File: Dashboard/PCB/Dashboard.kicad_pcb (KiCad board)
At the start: 4 copper layers, 96 parts, among them J1 Display, J2 Conn_01x26_Female, J3 LED, J7 PROGRAMMER, SW1 SW_SPST, U1 STM32F767ZIT6, U10 24LC01, U2 MP2359DJ-LF-Z, U3 MP2359DJ-LF-Z, U4 AS4C1M16S-6TCN, U5 AT25SF128A-SHB-T, U6 MP2332H, U7 MCP2561-E-SN, U8 MCP2561-E-SN, U9 ESP-12S, Y1 Crystal_GND24

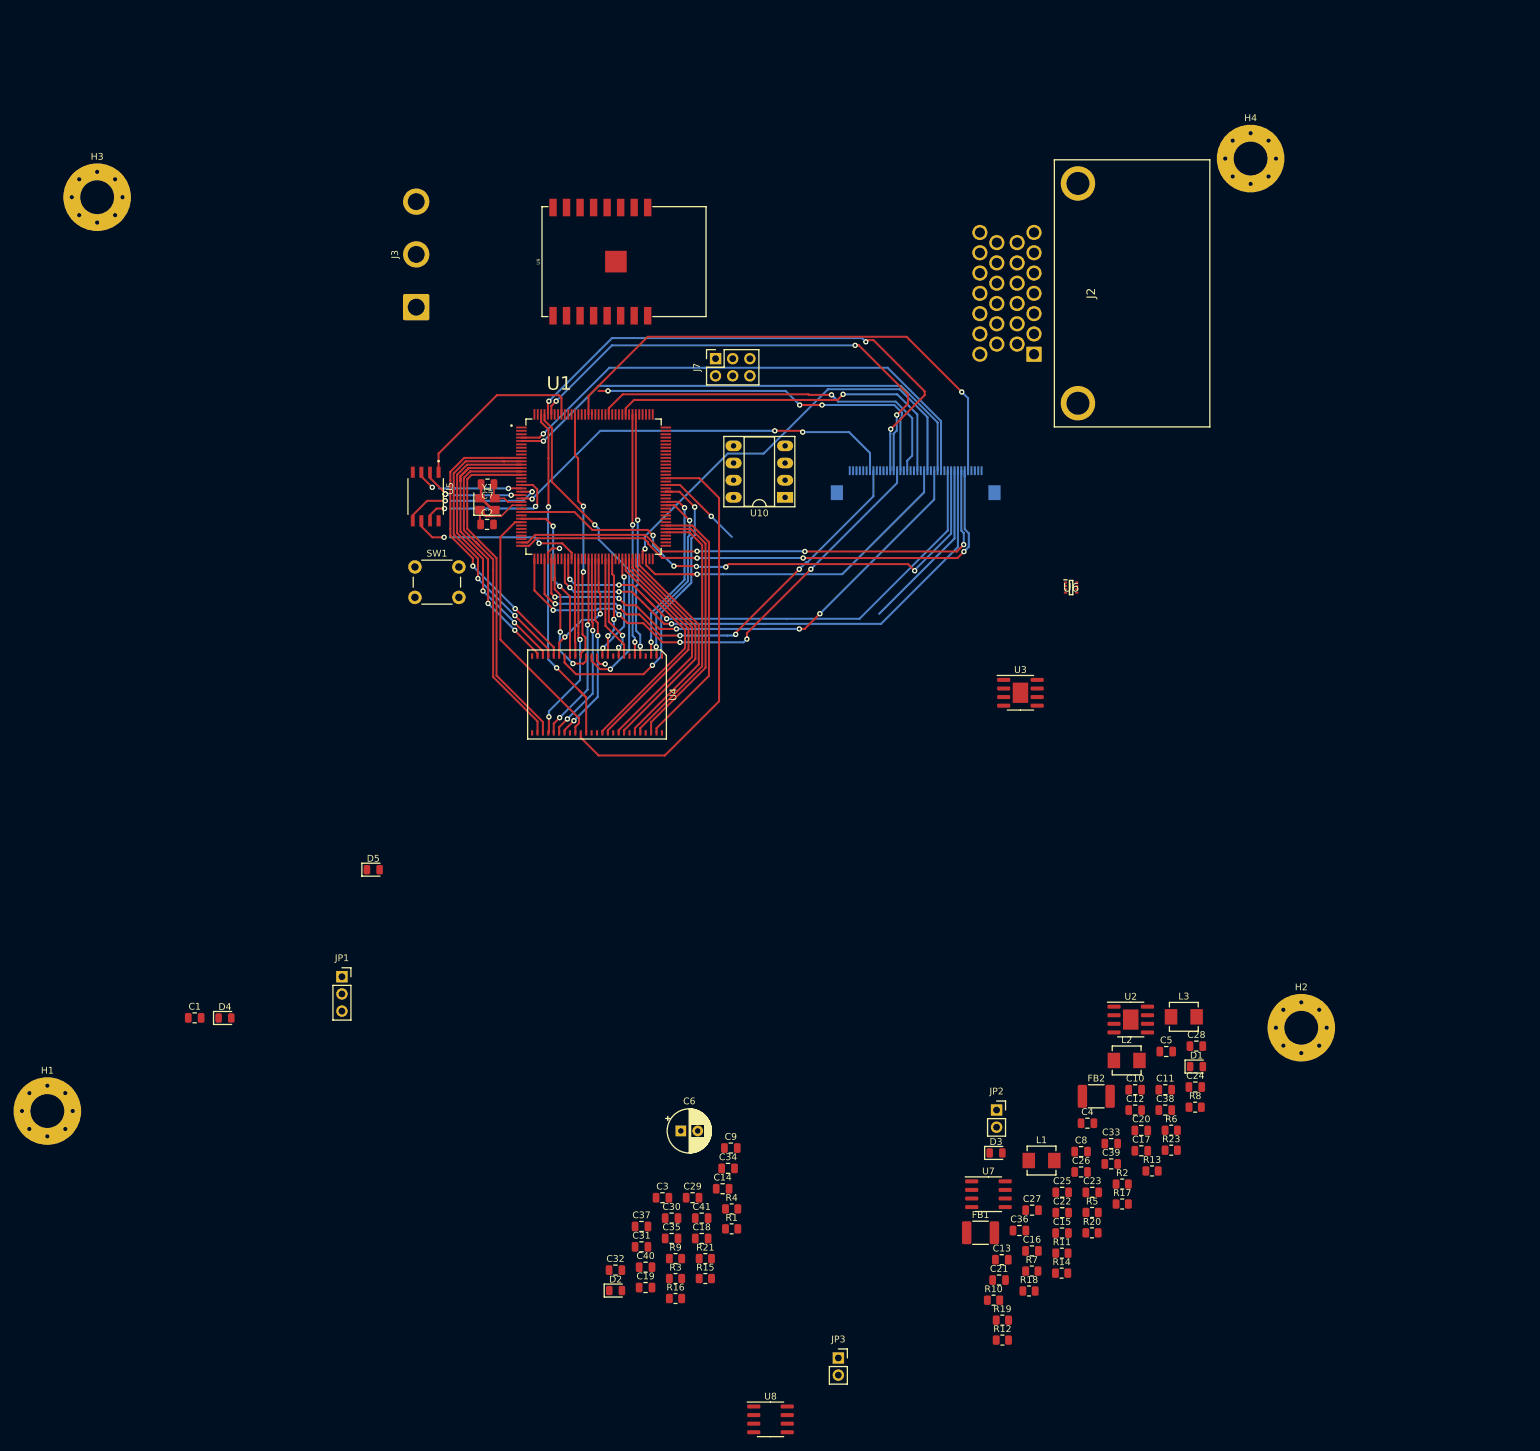
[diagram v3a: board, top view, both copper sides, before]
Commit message: New pcb board
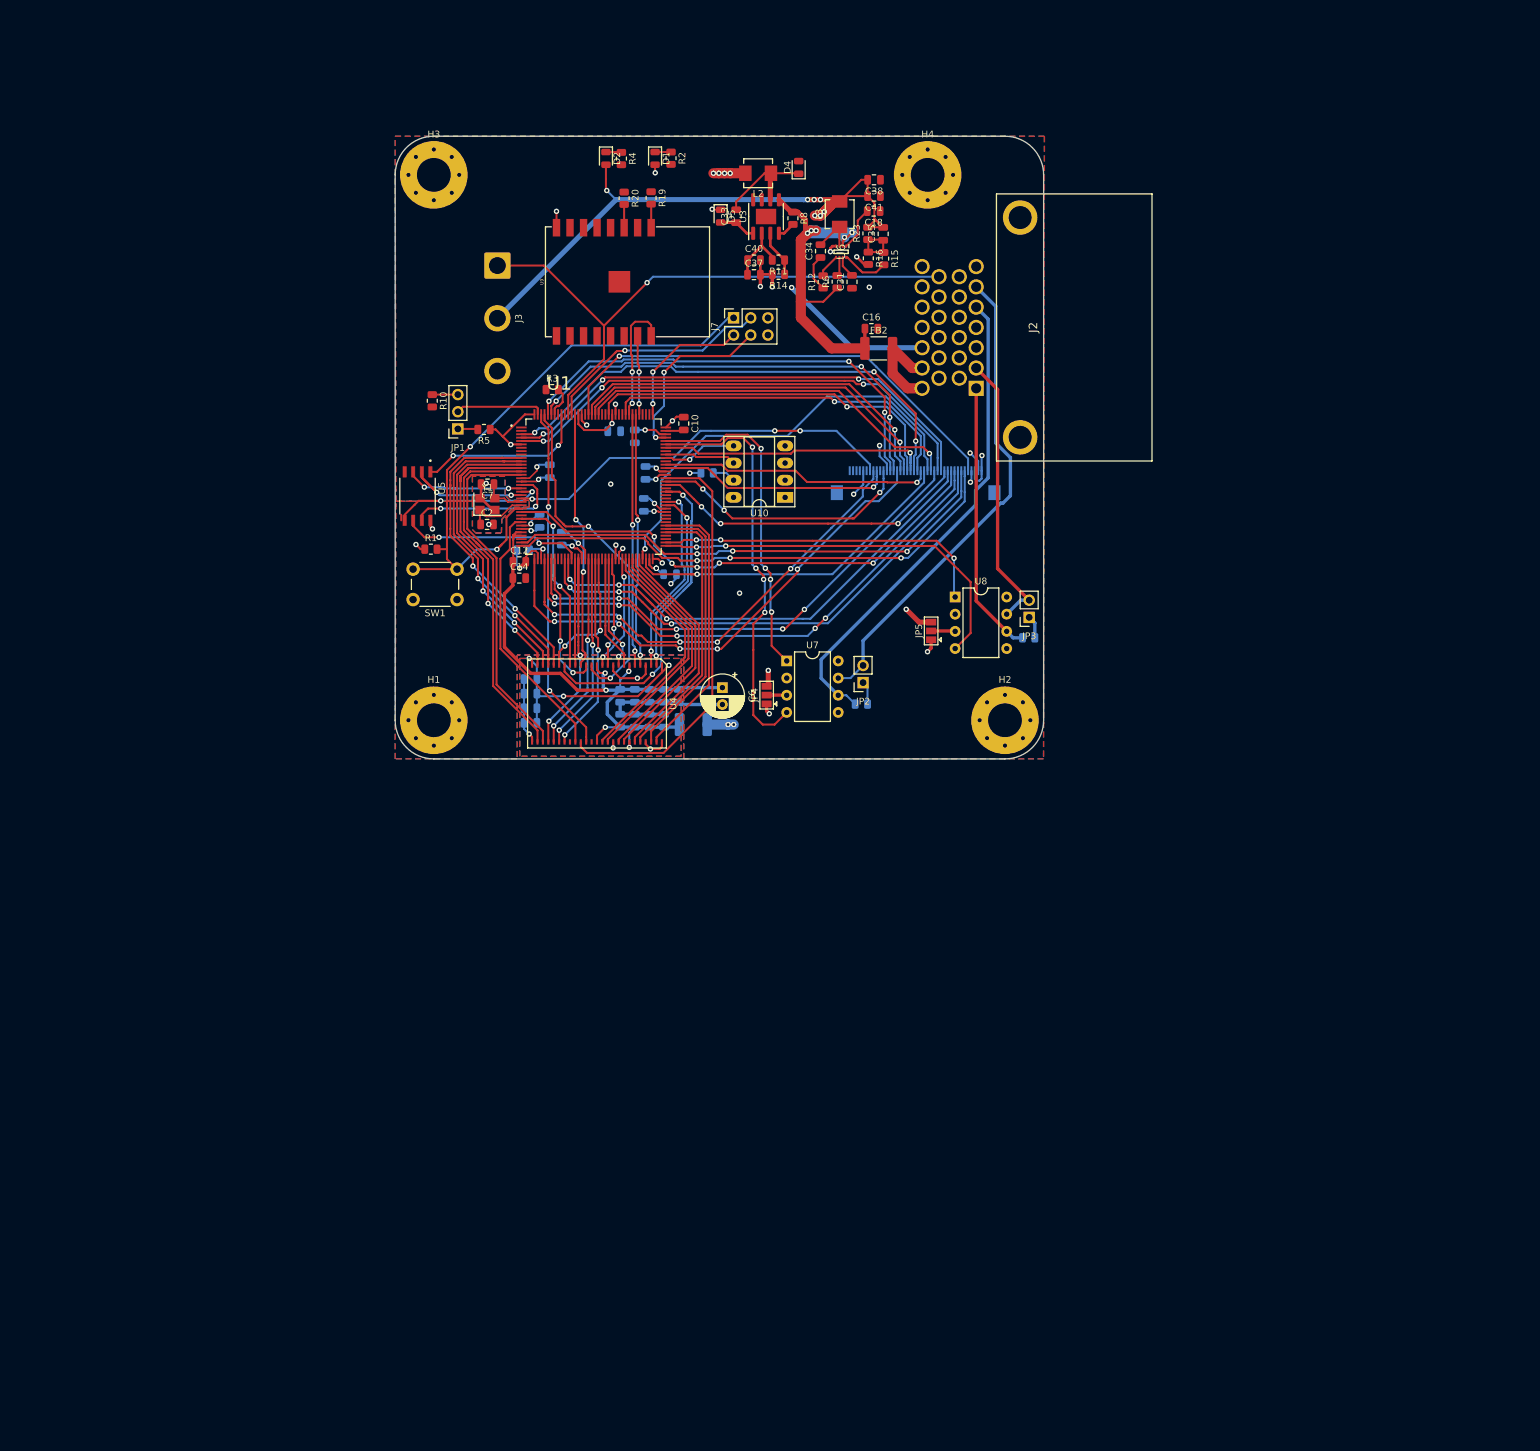
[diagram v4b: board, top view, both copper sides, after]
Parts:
- removed C32: 10nF, Capacitor_SMD:C_0805_2012Metric
- removed C36, C39: 10uF, Capacitor_SMD:C_0805_2012Metric
- removed D3: D_Schottky, Diode_SMD:D_0805_2012Metric
- removed L1: 10uH, Inductor_SMD:L_Vishay_IHLP-1616
- removed R13, R9: R, Resistor_SMD:R_0805_2012Metric
- removed R7: 100k, Resistor_SMD:R_0805_2012Metric
- removed U2: MP2359DJ-LF-Z, Package_SO:SOIC-8-1EP_3.9x4.9mm_P1.27mm_EP2.29x3mm
- added G***: LOGO, PGR_logo:logo_big, B.Cu at (133.1, 71.1)
- added JP4: Jumper_3_Bridged12, Jumper:SolderJumper-3_P1.3mm_Open_Pad1.0x1.5mm, F.Cu at (152.1, 111.9)
- added JP5: Jumper_3_Bridged12, Jumper:SolderJumper-3_P1.3mm_Open_Pad1.0x1.5mm, F.Cu at (176.4, 102.4)
- C1, C11, C13, C15, C17, C19, C20, C21, C22, C23, C24, C25, C26, C27, C28, C29, C3, C30, C4, C5, C8, C9, FB1, R17, R18, R21: moved to B.Cu
- U7, U8: footprint Package_SO:SOIC-8_3.9x4.9mm_P1.27mm -> Package_DIP:DIP-8_W7.62mm
- moved R19 173.9 mm to (135.0, 38.3), turned to 270 degrees
- moved R20 167.9 mm to (131.0, 38.4), turned to 270 degrees
- moved D2 167.4 mm to (128.3, 32.5), turned to 270 degrees
- moved R2 165.7 mm to (137.9, 32.5), turned to 270 degrees
- moved R12 158.7 mm to (160.4, 50.7), turned to 90 degrees
- moved R10 156.8 mm to (102.6, 68.3), turned to 270 degrees
- moved R16 156.4 mm to (167.1, 47.3), turned to 270 degrees
- moved D1 156.3 mm to (135.6, 32.5), turned to 270 degrees
- moved R4 156.2 mm to (130.6, 32.5), turned to 270 degrees
- moved C18 154.0 mm to (167.9, 40.3), turned to 180 degrees
- moved R14 153.5 mm to (153.8, 49.6), turned to 180 degrees
- moved C41 153.3 mm to (168.0, 38.1), turned to 180 degrees
- moved R15 153.1 mm to (169.4, 47.3), turned to 270 degrees
- moved R11 152.7 mm to (153.8, 47.5), turned to 180 degrees
- moved C35 151.8 mm to (169.3, 43.6), turned to 90 degrees
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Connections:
- J2 pad 1: Net-(J2-Pad1) -> CAN_L2
- J2 pad 12: GND -> Net-(J2-Pad12)
- J2 pad 13: GND -> Net-(J2-Pad13)
- J2 pad 15: +3V3 -> Net-(J2-Pad15)
- J2 pad 16: +5V -> Net-(J2-Pad16)
- J2 pad 17: +12V -> Net-(J2-Pad17)
- J2 pad 18: +12V -> Net-(J2-Pad18)
- J2 pad 19: Net-(J2-Pad19) -> LED_DATA
- J2 pad 2: Net-(J2-Pad2) -> CAN_H2
- J2 pad 22: Net-(J2-Pad22) -> GND
- J2 pad 23: CAN_L2 -> +3V3
- J2 pad 24: CAN_H2 -> +5V
- J2 pad 25: CAN_L1 -> +12V
- J2 pad 26: CAN_H1 -> +12V
- J2 pad 5: Net-(J2-Pad5) -> CAN_L1
- J2 pad 6: Net-(J2-Pad6) -> CAN_H1
- U7 pad 3: +5V -> Net-(JP4-Pad2)
- U8 pad 3: +5V -> Net-(JP5-Pad2)
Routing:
- net +5V: track 0.00 -> 255.2 mm, vias 0 -> 11
- net +3V3: track 0.00 -> 119.0 mm, vias 0 -> 30
- net GND: track 5.40 -> 122.4 mm, vias 0 -> 25
- net RST: track 0.00 -> 91.1 mm, vias 0 -> 2
- net +3.3VA: track 2.10 -> 91.8 mm, vias 1 -> 5
- net LED_DATA: track 0.00 -> 87.3 mm, vias 0 -> 1
- net /LTDC_B0: track 0.00 -> 73.9 mm, vias 0 -> 3
- net CAN_L1: track 0.00 -> 72.4 mm
- net CAN_H1: track 0.00 -> 71.8 mm
- net CAN_1_2: track 0.00 -> 61.1 mm, vias 0 -> 4
- net +12L: track 0.00 -> 59.8 mm, vias 0 -> 5
- net CAN_2_2: track 0.00 -> 58.2 mm, vias 0 -> 2
- net /LTDC_G3: track 0.00 -> 58.0 mm, vias 0 -> 1
- net /LTDC_B3: track 0.00 -> 55.2 mm, vias 0 -> 1
- net /LTDC_R4: track 28.7 -> 79.9 mm, vias 1 -> 5
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- added copper zone on In2.Cu, net +3V3
- added copper zone on B.Cu, net GND
- added copper zone on F.Cu, net GND
- added copper zone on In1.Cu, net GND
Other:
- board outline added: 95.9 x 92.1 mm
- board text added: "M. NADARZYNSKI"

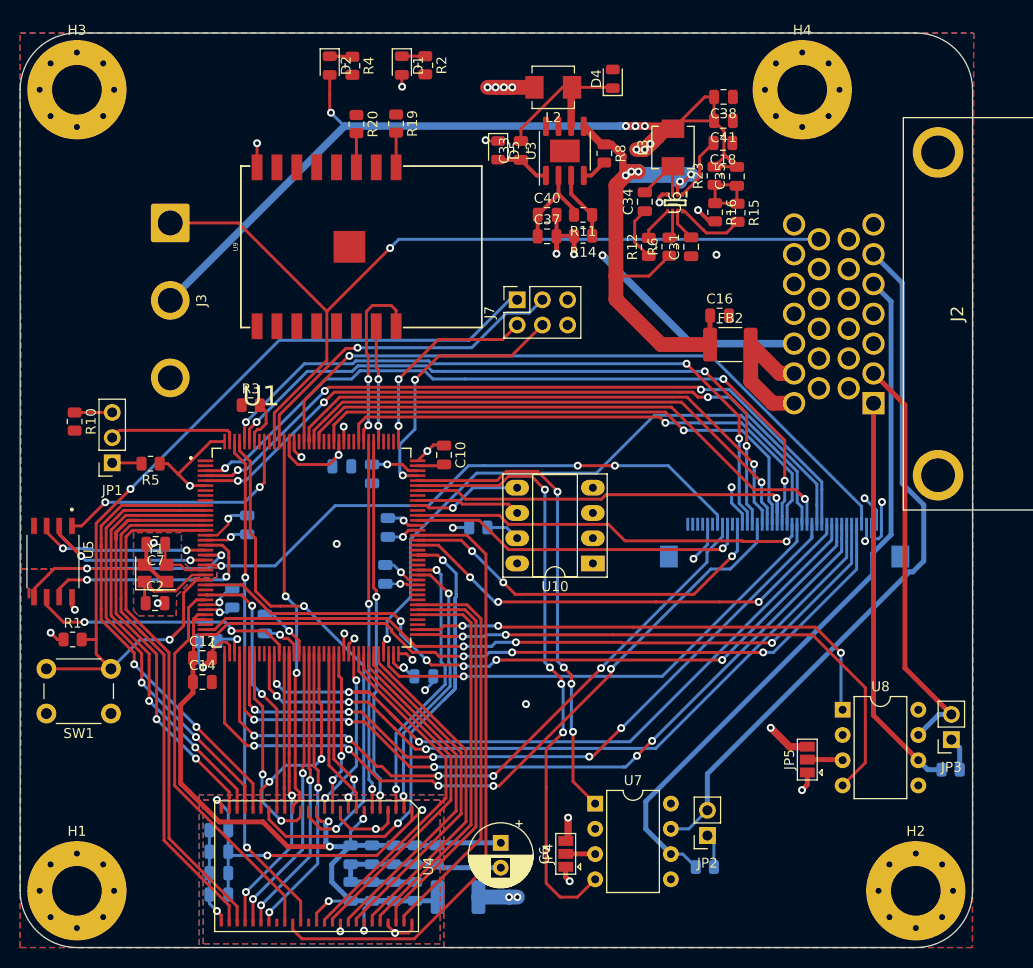
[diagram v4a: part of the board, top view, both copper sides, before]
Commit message: Add signal led
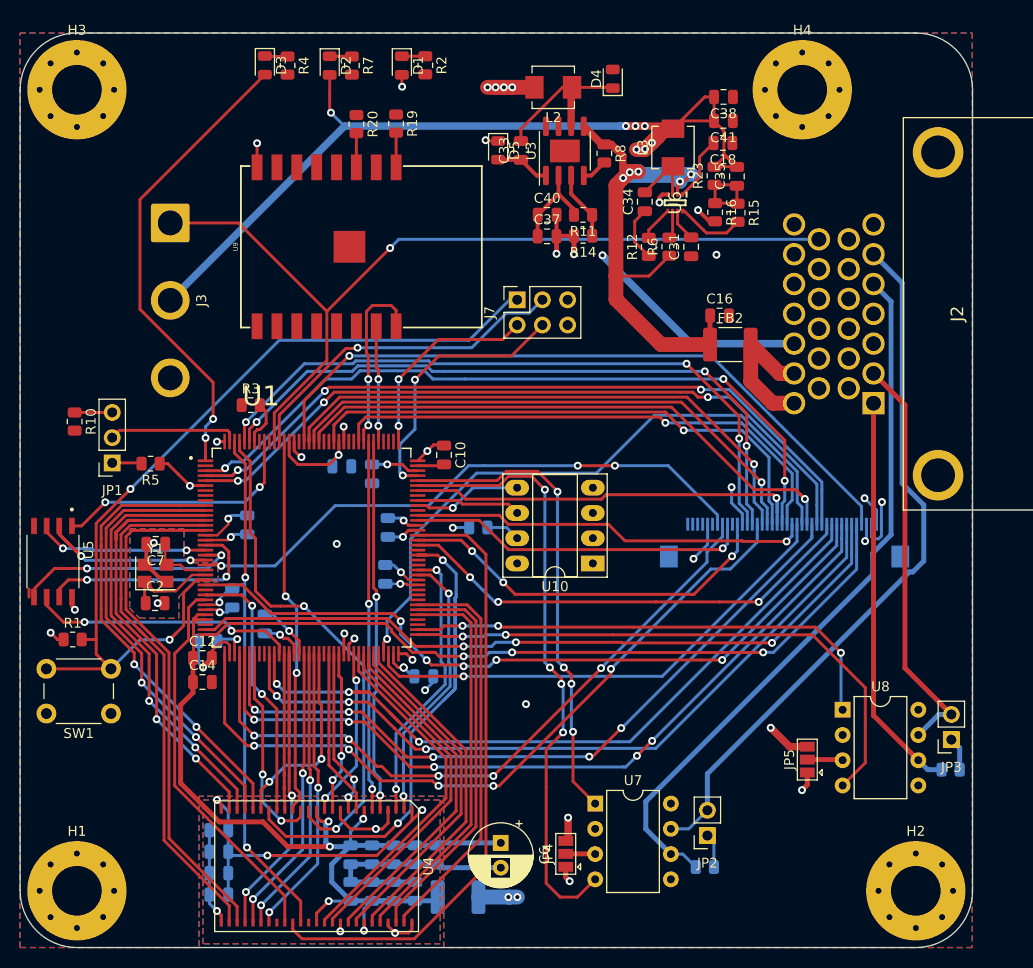
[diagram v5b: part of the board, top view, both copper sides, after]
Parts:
- added D3: LED_5V, LED_SMD:LED_0805_2012Metric, F.Cu at (121.8, 32.5)
- added R7: R, Resistor_SMD:R_0805_2012Metric, F.Cu at (130.6, 32.5)
- moved R4 6.53 mm to (124.1, 32.5)
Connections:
- R4 pad 1: Net-(D2-Pad1) -> Net-(D3-Pad1)
- U1 pad 1: Net-(U1-Pad1) -> SIGNAL_LED
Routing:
- net SIGNAL_LED: track 0.00 -> 47.5 mm, vias 0 -> 2
- net +3V3: track 119.0 -> 113.7 mm, vias 30 -> 31
- net Net-(D3-Pad1): track 0.00 -> 2.31 mm
